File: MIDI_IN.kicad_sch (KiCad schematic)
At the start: 6 parts, among them J28 Conn_01x03, U2 H11L1M

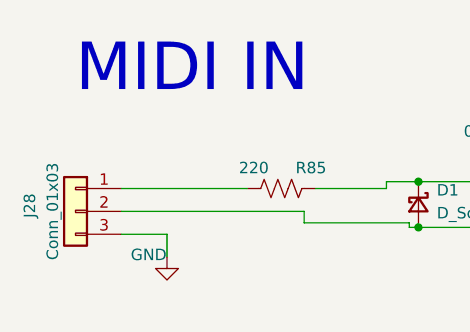
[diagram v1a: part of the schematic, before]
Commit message: simplified design, rely on external boards more to cover those cases
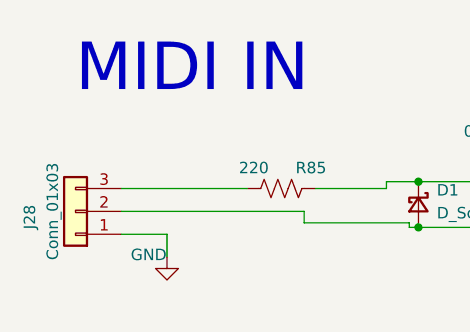
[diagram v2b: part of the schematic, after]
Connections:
- net GND: now also J28.1 (Pin_1); no longer J28.3 (Pin_3)
- net at R85.2: now also J28.3 (Pin_3); no longer J28.1 (Pin_1)
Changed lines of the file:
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@@
-    )
-  )
-  (symbol (lib_id "4ms_Connector:Conn_01x03") (at 87.63 85.09 0) (mirror y) (unit 1)
-    (in_bom yes) (on_board yes) (dnp no)
-    (property "Reference" "J28" (at 82.55 84.455 90)
-      (effects (font (size 1.27 1.27)))
-    )
-    (property "Value" "Conn_01x03" (at 85.09 85.09 90)
-      (effects (font (size 1.27 1.27)))
-    )
-    (property "Footprint" "Ultralibrarian:PinHeader_1x03_P2.54mm_Vertical_Female" (at 87.63 78.105 0)
-      (effects (font (size 1.27 1.27)) hide)
-    )
-    (property "Datasheet" "" (at 87.63 85.09 0)
-      (effects (font (size 1.27 1.27)) hide)
-    )
-    (property "Specifications" "HEADER 1x3 MALE PINS 0.100” 180deg" (at 90.17 92.964 0)
-      (effects (font (size 1.27 1.27)) (justify left) hide)
-    )
-    (property "Manufacturer" "TAD" (at 90.17 94.488 0)
-      (effects (font (size 1.27 1.27)) (justify left) hide)
-    )
-    (property "Part Number" "1-0301FBV0T" (at 90.17 96.012 0)
-      (effects (font (size 1.27 1.27)) (justify left) hide)
-    )
-    (pin "1")
-    (pin "2")
-    (pin "3")
-    (instances
-      (project "DaisySeedBreakout"
-        (path "/a83c9f4b-f61b-47d4-b39d-4636bff6eb0e"
-          (reference "J28") (unit 1)
-        )
-        (path "/a83c9f4b-f61b-47d4-b39d-4636bff6eb0e/0f869182-0545-465a-951d-d9d2cc6b23cc"
-          (reference "J3") (unit 1)
-        )
-      )
     )
   )
@@
         )
       )
+    )
+  )
+  (symbol (lib_id "4ms_Connector:Conn_01x03") (at 87.63 85.09 180) (unit 1)
+    (in_bom yes) (on_board yes) (dnp no)
+    (property "Reference" "J28" (at 82.55 85.725 90)
+      (effects (font (size 1.27 1.27)))
+    )
+    (property "Value" "Conn_01x03" (at 85.09 85.09 90)
+      (effects (font (size 1.27 1.27)))
+    )
+    (property "Footprint" "Ultralibrarian:PinHeader_1x03_P2.54mm_Vertical_Female" (at 87.63 92.075 0)
+      (effects (font (size 1.27 1.27)) hide)
+    )
+    (property "Datasheet" "" (at 87.63 85.09 0)
+      (effects (font (size 1.27 1.27)) hide)
+    )
+    (property "Specifications" "HEADER 1x3 MALE PINS 0.100” 180deg" (at 90.17 77.216 0)
+      (effects (font (size 1.27 1.27)) (justify left) hide)
+    )
+    (property "Manufacturer" "TAD" (at 90.17 75.692 0)
+      (effects (font (size 1.27 1.27)) (justify left) hide)
+    )
+    (property "Part Number" "1-0301FBV0T" (at 90.17 74.168 0)
+      (effects (font (size 1.27 1.27)) (justify left) hide)
+    )
+    (pin "1")
+    (pin "2")
+    (pin "3")
+    (instances
+      (project "DaisySeedBreakout"
+        (path "/a83c9f4b-f61b-47d4-b39d-4636bff6eb0e"
+          (reference "J28") (unit 1)
+        )
+        (path "/a83c9f4b-f61b-47d4-b39d-4636bff6eb0e/0f869182-0545-465a-951d-d9d2cc6b23cc"
+          (reference "J3") (unit 1)
+        )
+      )

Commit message: started layout
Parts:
- C32: footprint Capacitor_SMD:C_0603_1608Metric -> Capacitor_SMD:C_0402_1005Metric
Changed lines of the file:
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@@
       (effects (font (size 1.27 1.27)) (justify left))
     )
-    (property "Footprint" "Capacitor_SMD:C_0603_1608Metric" (at 137.668 74.93 0)
+    (property "Footprint" "Capacitor_SMD:C_0402_1005Metric" (at 137.668 74.93 0)
       (effects (font (size 1.27 1.27)) hide)
     )

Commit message: periodic update
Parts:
- J28: footprint Ultralibrarian:PinHeader_1x03_P2.54mm_Vertical_Female -> HeadersWithSolderHoles:PinHeader_1x03_P2.54mm_Vertical_Female_WithSolderHoles
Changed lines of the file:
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@@
       (effects (font (size 1.27 1.27)))
     )
-    (property "Footprint" "Ultralibrarian:PinHeader_1x03_P2.54mm_Vertical_Female" (at 87.63 92.075 0)
+    (property "Footprint" "HeadersWithSolderHoles:PinHeader_1x03_P2.54mm_Vertical_Female_WithSolderHoles" (at 87.63 92.075 0)
       (effects (font (size 1.27 1.27)) hide)
     )

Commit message: Layout routed, no DRC yet
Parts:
- J28: footprint HeadersWithSolderHoles:PinHeader_1x03_P2.54mm_Vertical_Female_WithSolderHoles -> FemaleHeaders:PinHeader_1x03_P2.54mm_Vertical_Female
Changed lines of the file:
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@@
       (effects (font (size 1.27 1.27)))
     )
-    (property "Footprint" "HeadersWithSolderHoles:PinHeader_1x03_P2.54mm_Vertical_Female_WithSolderHoles" (at 87.63 92.075 0)
+    (property "Footprint" "FemaleHeaders:PinHeader_1x03_P2.54mm_Vertical_Female" (at 87.63 92.075 0)
       (effects (font (size 1.27 1.27)) hide)
     )

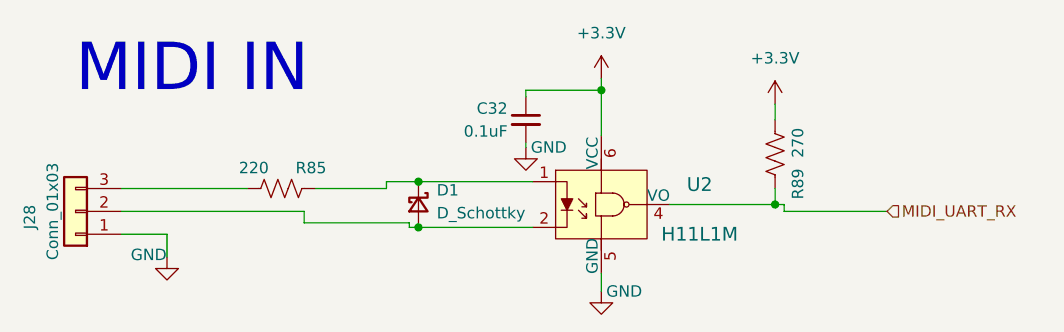
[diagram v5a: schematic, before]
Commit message: PCB cleanup, added accelerometer as easy sensor to begin with
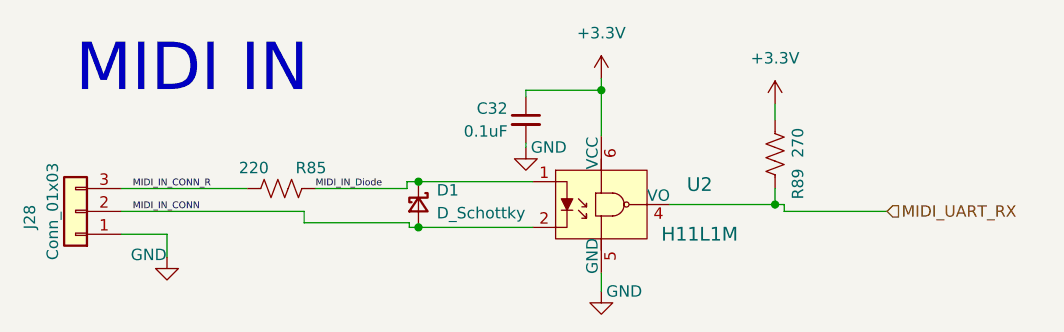
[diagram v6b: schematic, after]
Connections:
- net MIDI_IN_Diode: now reaches D1.1 (K), R85.1, U2.1
- net MIDI_IN_CONN_R: now reaches J28.3 (Pin_3), R85.2
- net MIDI_IN_CONN: now reaches D1.2 (A), J28.2 (Pin_2), U2.2
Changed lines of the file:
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@@
+    (stroke (width 0) (type default))
+  )
+  (wire (pts (xy 114.3 82.55) (xy 124.46 82.55))
     (stroke (width 0) (type default))
   )
@@
     (stroke (width 0) (type default))
   )
-  (wire (pts (xy 122.174 82.55) (xy 122.174 81.788))
-    (stroke (width 0) (type default))
-  )
-  (wire (pts (xy 114.3 82.55) (xy 122.174 82.55))
+  (wire (pts (xy 124.46 82.55) (xy 124.46 81.788))
     (stroke (width 0) (type default))
   )
@@
     (stroke (width 0) (type default))
   )
-  (wire (pts (xy 122.174 81.788) (xy 125.73 81.788))
+  (wire (pts (xy 124.46 81.788) (xy 125.73 81.788))
     (stroke (width 0) (type default))
   )
@@
     (effects (font (size 5.27 5.27)) (justify left bottom))
   )
+  (label "MIDI_IN_Diode" (at 114.3 82.55 0) (fields_autoplaced)
+    (effects (font (size 0.75 0.75)) (justify left bottom))
+  )
+  (label "MIDI_IN_CONN_R" (at 93.98 82.55 0) (fields_autoplaced)
+    (effects (font (size 0.75 0.75)) (justify left bottom))
+  )
+  (label "MIDI_IN_CONN" (at 93.98 85.09 0) (fields_autoplaced)
+    (effects (font (size 0.75 0.75)) (justify left bottom))
+  )
   (hierarchical_label "MIDI_UART_RX" (shape input) (at 177.8 85.09 0) (fields_autoplaced)
